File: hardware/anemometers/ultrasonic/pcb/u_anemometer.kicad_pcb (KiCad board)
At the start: 4 copper layers, 46 x 46 mm, 154 parts, among them Q1 SI2301CDS-T1-GE3, Q2 SI2301CDS-T1-GE3, SW1 B3U-1000P, U1 TCAN330GDCNR, U2 STM32L476RGT6, U3 XC6206P332MR, U4 MAX3222EIPWR, U5 SN74LV4052APW, U6 MAX3222EIPWR, U7 LMV358B-VR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

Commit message: Fixes!
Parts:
- removed C10, C11, C57: , ProDoc_1-PCB_PCB_2021-01-26_22-01-27_2026-01-16:C0402
- removed Q3: , ProDoc_1-PCB_PCB_2021-01-26_22-01-27_2026-01-16:SOT-23-3_L2.9-W1.3-P1.90-LS2.4-BR
- removed R44: , ProDoc_1-PCB_PCB_2021-01-26_22-01-27_2026-01-16:R0402
- moved ? 9.46 mm to (145.1, 103.4)
- moved REF** 0.41 mm to (138.4, 110.2)
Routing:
- net GND: track 241.0 -> 229.6 mm, vias 114 -> 110
- net V_OPA: track 20.7 -> 15.2 mm
- net RAIN_SENS: track 5.13 -> 0.00 mm
- net 3.3V: track 92.7 -> 90.1 mm, vias 18 -> 17
- net unconnected-(U2-PA1-Pad15): track 2.38 -> 0.00 mm
- net Q3_1: track 1.55 -> 0.00 mm

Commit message: Fab updates
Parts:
- removed C53: , ProDoc_1-PCB_PCB_2021-01-26_22-01-27_2026-01-16:C0402
- removed U10: , ProDoc_1-PCB_PCB_2021-01-26_22-01-27_2026-01-16:ADPS-9250
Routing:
- net GND: track 229.6 -> 224.1 mm
- net SCL: track 55.8 -> 52.2 mm
- net SDA: track 59.1 -> 57.2 mm
- net 3.3V: track 90.1 -> 88.3 mm, vias 17 -> 16

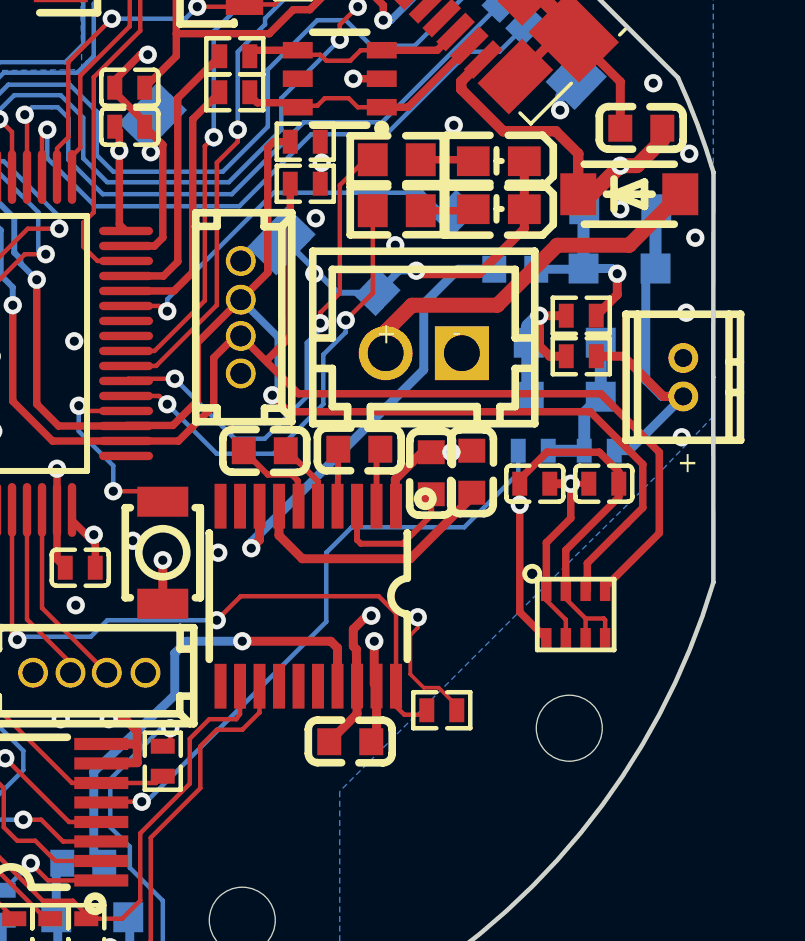
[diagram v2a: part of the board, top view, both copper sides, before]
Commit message: Remove BME280
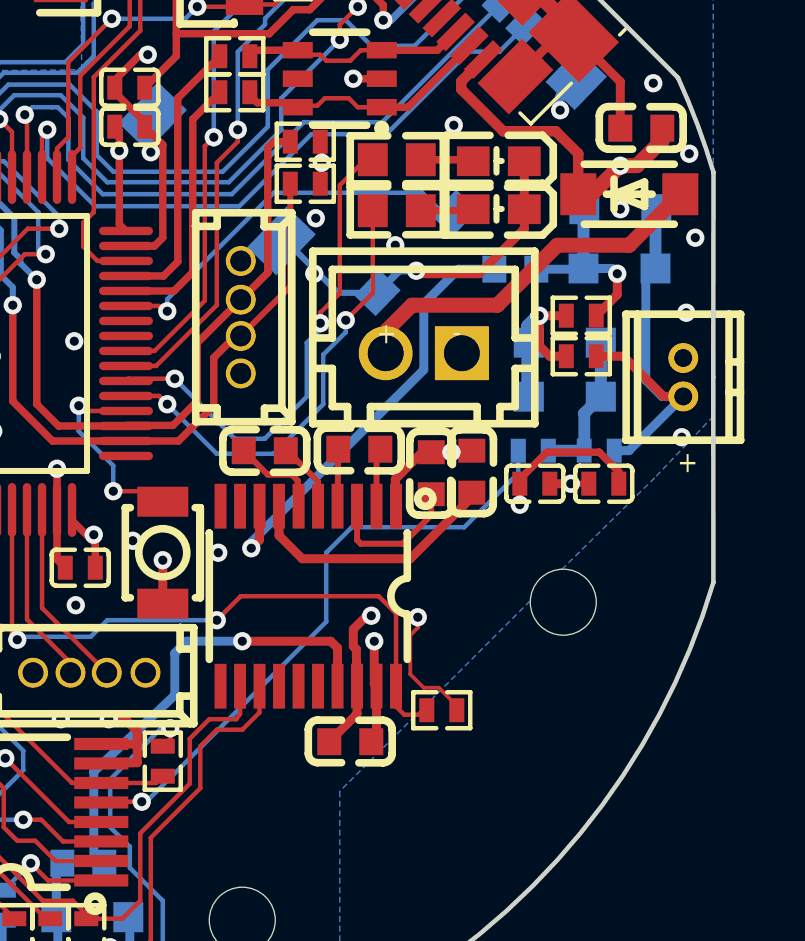
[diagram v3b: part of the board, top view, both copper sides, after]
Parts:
- removed U8: BME280, ProDoc_1-PCB_PCB_2021-01-26_22-01-27_2026-01-16:LGA-8_BME280_BR
- LED1: value 19-217/BHC-ZL1M2RY/3T -> XL-1608UBC-06A
- U5: value SN74LV4052APW -> TMUX4052PWR
- U9: value BMX160 -> BMI270
- VBAT1: value (none) -> 4.7uF
- moved REF** 4.20 mm to (168.0, 117.5)
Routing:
- net SDA: track 57.2 -> 35.1 mm, vias 5 -> 4
- net SCL: track 52.2 -> 30.9 mm
- net 3.3V: track 88.3 -> 76.0 mm
- net GND: track 224.1 -> 218.3 mm

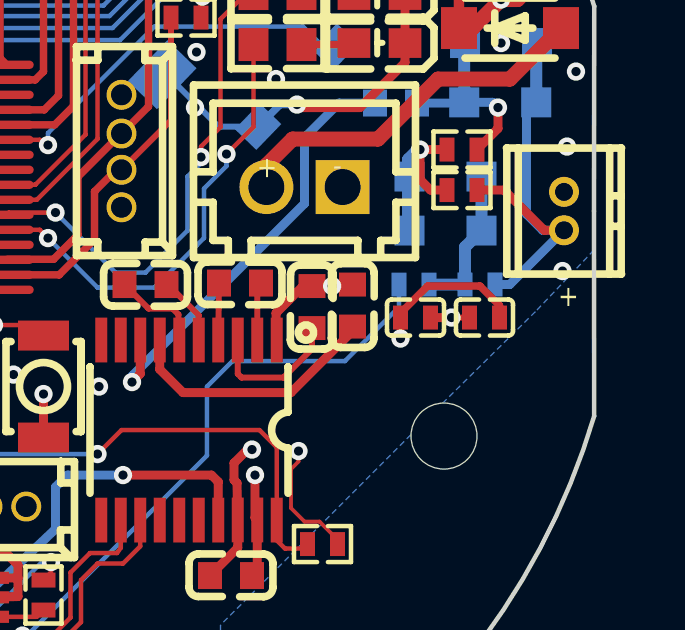
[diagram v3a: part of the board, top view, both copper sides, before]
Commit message: Delete c47 and C50
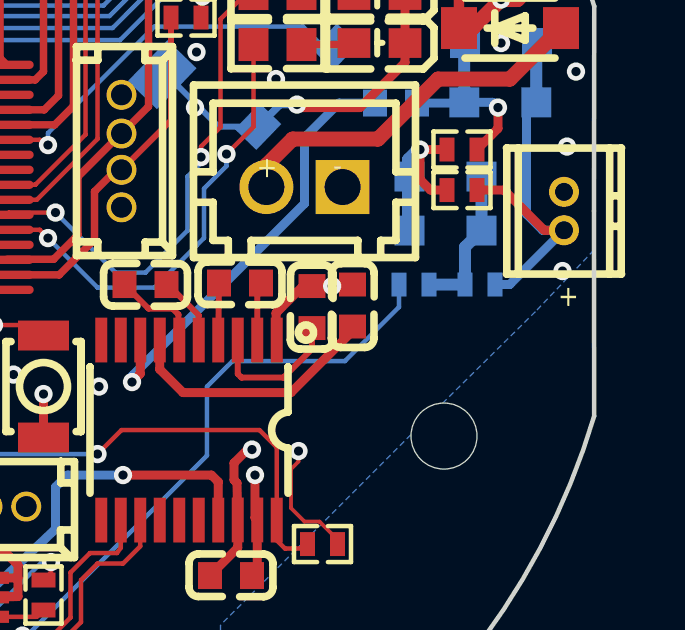
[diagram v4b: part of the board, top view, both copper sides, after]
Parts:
- removed C47, C50: 100nF, ProDoc_1-PCB_PCB_2021-01-26_22-01-27_2026-01-16:C0402
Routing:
- net 3.3V: track 76.0 -> 70.9 mm, vias 16 -> 15
- net GND: track 218.3 -> 216.4 mm, vias 110 -> 109

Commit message: blank board
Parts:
- removed REF** (x3): MountingHole_2.2mm_M2_ISO14580, MountingHole:MountingHole_2.2mm_M2_ISO14580
- moved C29 58.0 mm to (189.4, 105.5)
- moved C34 58.0 mm to (185.9, 100.0)
- moved C37 58.0 mm to (218.9, 106.6)
- moved C39 58.0 mm to (196.7, 124.0)
- moved C43 58.0 mm to (222.7, 107.3)
- moved C5 58.0 mm to (188.9, 94.4)
- moved C6 58.0 mm to (188.9, 96.8)
- moved C7 58.0 mm to (188.9, 98.3)
- moved C9 58.0 mm to (197.8, 94.4)
- moved D1 58.0 mm to (198.4, 84.2)
- moved D11 58.0 mm to (204.7, 87.4)
- moved D18 58.0 mm to (204.4, 124.2)
- moved D19 58.0 mm to (204.4, 122.0)
- moved D3 58.0 mm to (227.9, 98.1)
- moved D5 58.0 mm to (227.6, 100.6)
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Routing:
- net GND: track 216.4 -> 0.00 mm, vias 109 -> 0
- net +5V: track 75.6 -> 0.00 mm, vias 2 -> 0
- net 3.3V: track 70.9 -> 0.00 mm, vias 15 -> 0
- net /2_anemometer/SOUTH_IN: track 68.9 -> 0.00 mm, vias 1 -> 0
- net Net-(U4-DOUT1): track 41.4 -> 0.00 mm, vias 3 -> 0
- net /1_mcu/USART3_TX: track 40.9 -> 0.00 mm, vias 3 -> 0
- net /1_mcu/USART3_RX: track 39.3 -> 0.00 mm, vias 3 -> 0
- net SDA: track 35.1 -> 0.00 mm, vias 4 -> 0
- net /2_anemometer/WEST_IN: track 32.0 -> 0.00 mm, vias 1 -> 0
- net ECHO_OUT: track 31.7 -> 0.00 mm, vias 2 -> 0
- net SCL: track 30.9 -> 0.00 mm, vias 1 -> 0
- net /2_anemometer/SOUTH_OUT: track 29.2 -> 0.00 mm, vias 2 -> 0
- net /2_anemometer/WEST_OUT: track 28.5 -> 0.00 mm, vias 2 -> 0
- net /1_mcu/SDMMC1_CMD: track 26.1 -> 0.00 mm, vias 1 -> 0
- net /1_mcu/SDMMC1_CK: track 23.5 -> 0.00 mm, vias 3 -> 0
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- removed copper zone on In2.Cu, net 3.3V
- removed copper zone on B.Cu, net GND
- removed copper zone on In1.Cu, net GND
